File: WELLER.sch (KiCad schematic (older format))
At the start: 0 parts

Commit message: duży update, drc przechodzi
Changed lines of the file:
@@
 EESchema Schematic File Version 4
 LIBS:WELLER-cache
-EELAYER 26 0
+EELAYER 29 0
 EELAYER END
 $Descr A4 11693 8268
@@
 	6300 4600 2600 4600
 Wire Wire Line
-	2600 4600 2600 2950
+	2600 4600 2600 3100
 Wire Wire Line
 	2100 2950 2600 2950
@@
 F9 "termocouple" I R 5500 3550 50
 F10 "weller_con1" B R 5500 3200 50
+F11 "12V" I L 3750 3100 50
 $EndSheet
 Wire Wire Line
@@
 Wire Wire Line
 	5500 3550 6650 3550
+Wire Wire Line
+	2600 3100 3750 3100
+Connection ~ 2600 3100
+Wire Wire Line
+	2600 3100 2600 2950
 $EndSCHEMATC

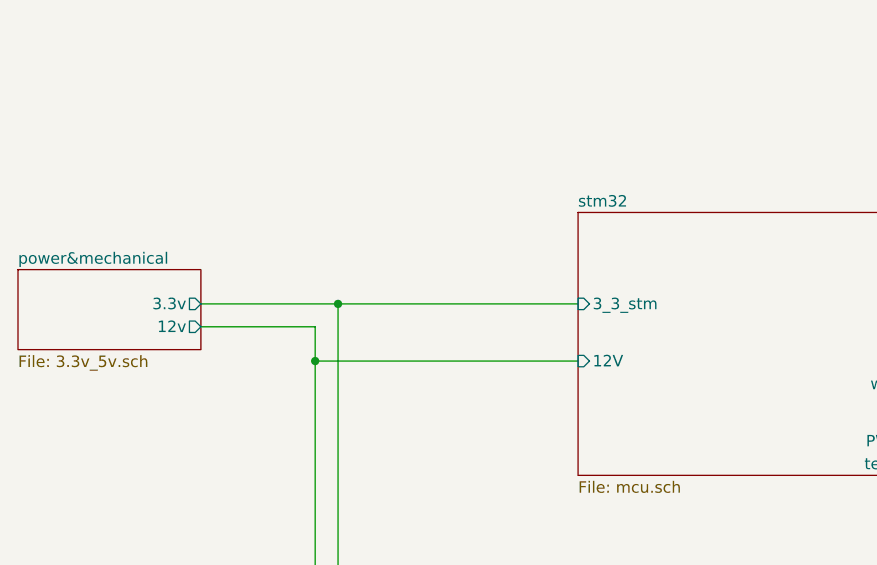
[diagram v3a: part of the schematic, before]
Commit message: dodanie pomiaru napięcia zasilającego grzałkę
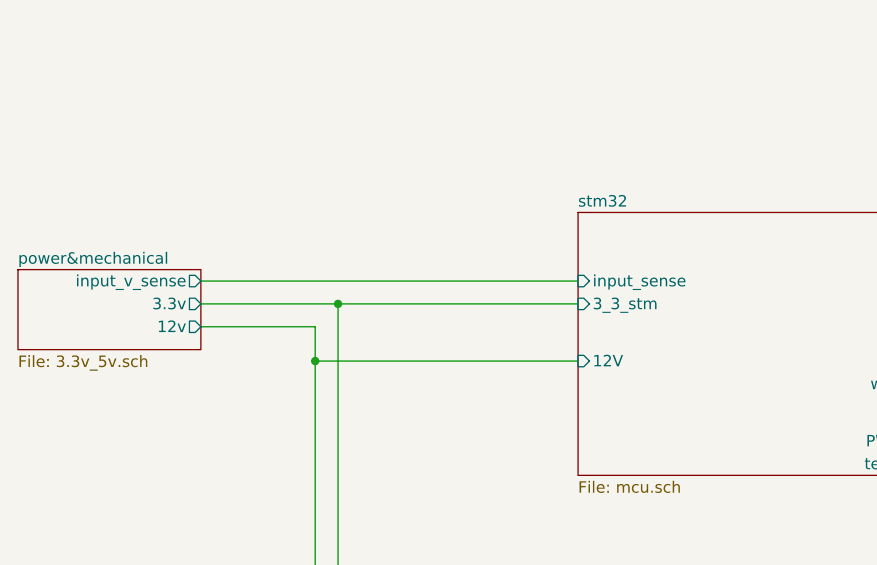
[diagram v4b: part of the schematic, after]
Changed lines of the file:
@@
 F2 "3.3v" O R 2100 2850 50
 F3 "12v" O R 2100 2950 50
+F4 "input_v_sense" O R 2100 2750 50
 $EndSheet
 $Sheet
@@
 F10 "weller_con1" B R 5500 3200 50
 F11 "12V" I L 3750 3100 50
+F12 "input_sense" I L 3750 2750 50
 $EndSheet
 Wire Wire Line
@@
 Wire Wire Line
 	2600 3100 2600 2950
+Wire Wire Line
+	3750 2750 2100 2750
 $EndSCHEMATC
